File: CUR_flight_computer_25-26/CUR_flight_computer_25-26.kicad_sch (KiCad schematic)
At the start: 0 parts

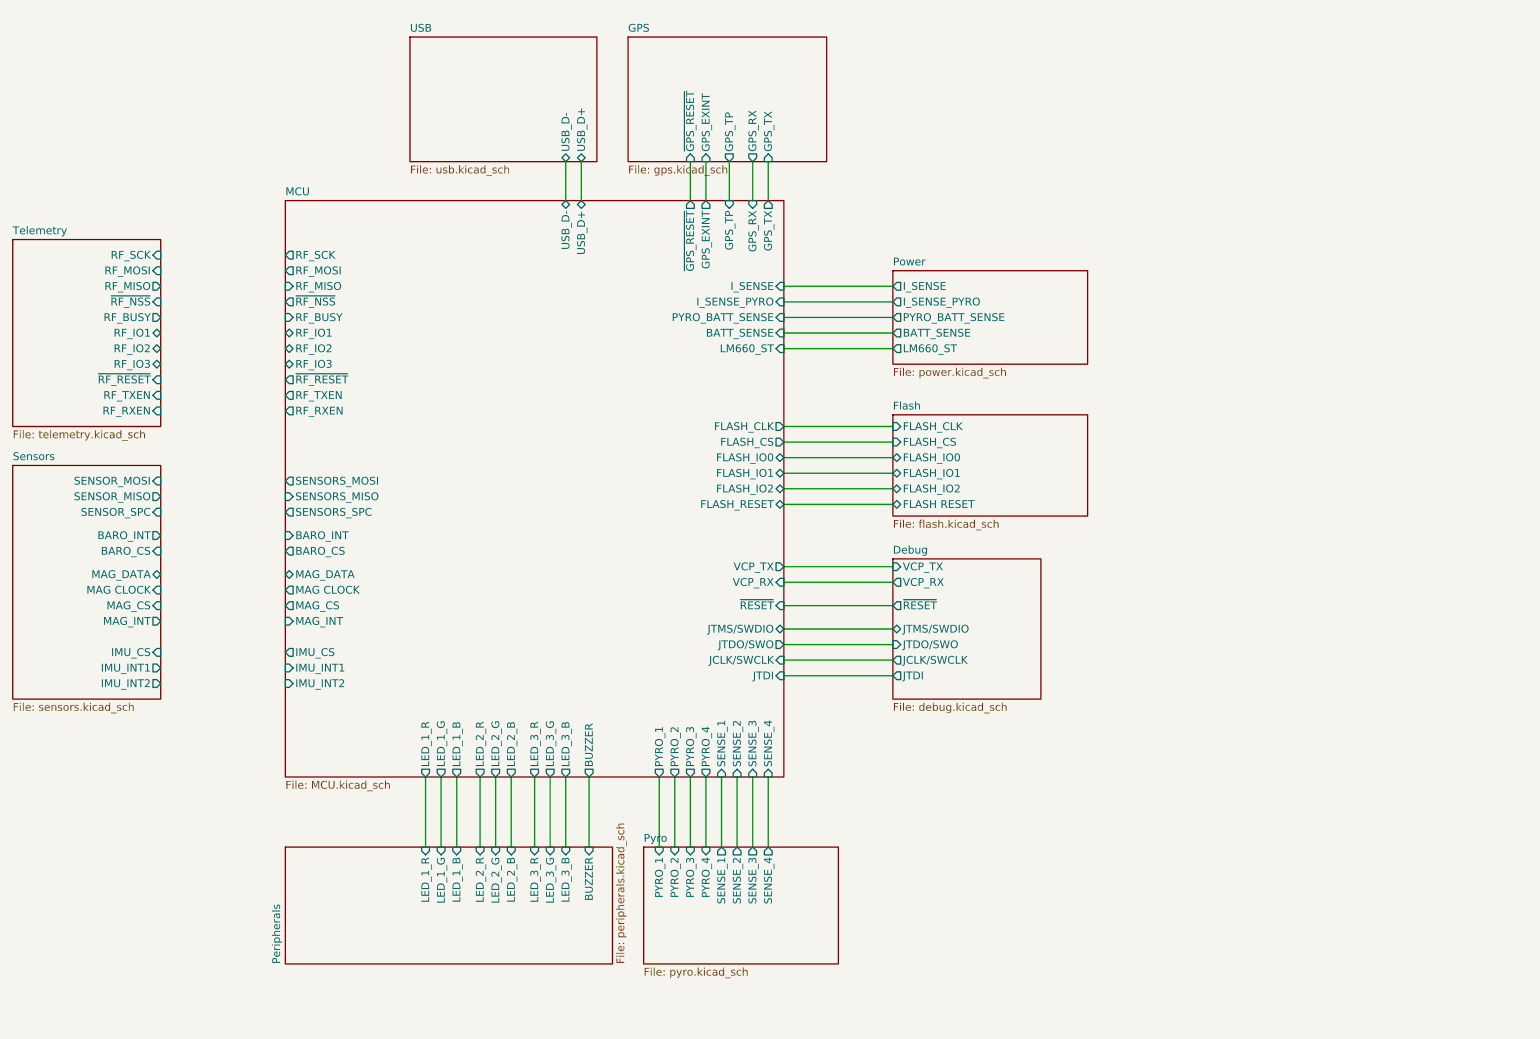
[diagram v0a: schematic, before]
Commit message: added SD_card holder
may need to confirm no pull up resistor required
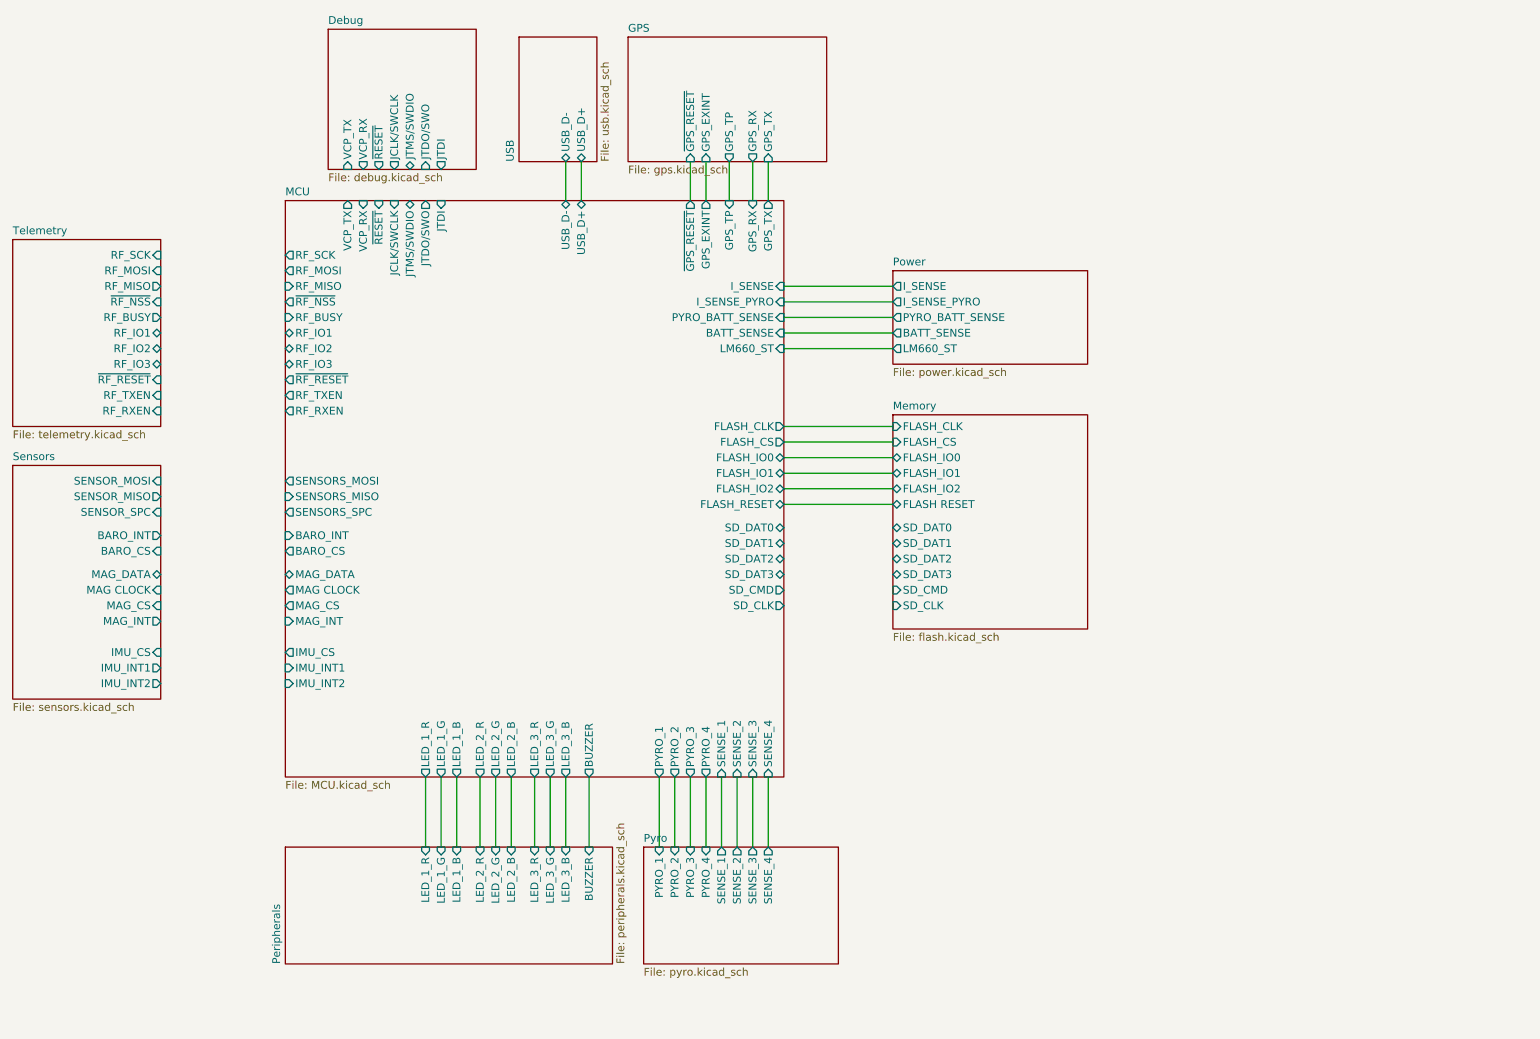
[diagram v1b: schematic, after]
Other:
- sheet Flash renamed Memory
- sheet MCU ports: added SD_CLK, SD_CMD, SD_DAT0, SD_DAT1, SD_DAT2, SD_DAT3; removed none
- sheet Memory ports: added SD_CLK, SD_CMD, SD_DAT0, SD_DAT1, SD_DAT2, SD_DAT3; removed none
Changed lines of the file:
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@@
-	(wire
-		(pts
-			(xy 162.56 105.41) (xy 180.34 105.41)
-		)
-		(stroke
-			(width 0)
-			(type default)
-		)
-	)
 	(wire
 		(pts
@@
 	(wire
 		(pts
-			(xy 162.56 111.76) (xy 180.34 111.76)
-		)
-		(stroke
-			(width 0)
-			(type default)
-		)
-	)
-	(wire
-		(pts
 			(xy 129.54 39.37) (xy 129.54 45.72)
 		)
@@
 	(wire
 		(pts
-			(xy 162.56 118.11) (xy 180.34 118.11)
-		)
-		(stroke
-			(width 0)
-			(type default)
-		)
-	)
-	(wire
-		(pts
 			(xy 124.46 139.7) (xy 124.46 151.13)
 		)
@@
 	(wire
 		(pts
-			(xy 162.56 123.19) (xy 180.34 123.19)
-		)
-		(stroke
-			(width 0)
-			(type default)
-		)
-	)
-	(wire
-		(pts
 			(xy 154.94 139.7) (xy 154.94 151.13)
 		)
@@
 	(wire
 		(pts
-			(xy 162.56 115.57) (xy 180.34 115.57)
-		)
-		(stroke
-			(width 0)
-			(type default)
-		)
-	)
-	(wire
-		(pts
 			(xy 180.34 59.69) (xy 162.56 59.69)
 		)
@@
 	(wire
 		(pts
-			(xy 162.56 120.65) (xy 180.34 120.65)
-		)
-		(stroke
-			(width 0)
-			(type default)
-		)
-	)
-	(wire
-		(pts
 			(xy 162.56 87.63) (xy 180.34 87.63)
 		)
@@
 	(wire
 		(pts
-			(xy 162.56 107.95) (xy 180.34 107.95)
-		)
-		(stroke
-			(width 0)
-			(type default)
-		)
-	)
-	(wire
-		(pts
 			(xy 127 139.7) (xy 127 151.13)
 		)
@@
 	)
 	(sheet
-		(at 180.34 104.14)
+		(at 88.265 17.78)
 		(size 24.13 22.86)
 		(exclude_from_sim no)
@@
 		)
 		(property "Sheetname" "Debug"
-			(at 180.34 103.4284 0)
+			(at 88.265 17.0684 0)
 			(effects
 				(font
@@
 		)
 		(property "Sheetfile" "debug.kicad_sch"
-			(at 180.34 127.5846 0)
+			(at 88.265 41.2246 0)
 			(effects
 				(font
@@
 		)
 		(pin "VCP_TX" input
-			(at 180.34 105.41 180)
+			(at 91.44 40.64 270)
 			(effects
 				(font
@@
 		)
 		(pin "JTDI" output
-			(at 180.34 123.19 180)
+			(at 106.68 40.64 270)
 			(effects
 				(font
@@
 		)
 		(pin "~{RESET}" output
-			(at 180.34 111.76 180)
+			(at 96.52 40.64 270)
 			(effects
 				(font
@@
 		)
 		(pin "JTMS/SWDIO" bidirectional
-			(at 180.34 115.57 180)
+			(at 101.6 40.64 270)
 			(effects
 				(font
@@
 		)
 		(pin "JTDO/SWO" input
-			(at 180.34 118.11 180)
+			(at 104.14 40.64 270)
 			(effects
 				(font
@@
 		)
 		(pin "JCLK/SWCLK" output
-			(at 180.34 120.65 180)
+			(at 99.06 40.64 270)
 			(effects
 				(font
@@
 		)
 		(pin "VCP_RX" output
-			(at 180.34 107.95 180)
+			(at 93.98 40.64 270)
 			(effects
 				(font
@@
 			)
 		)
-		(pin "VCP_TX" output
-			(at 162.56 105.41 0)
-			(effects
-				(font
-					(size 1.27 1.27)
-				)
-				(justify right)
-			)
-		)
-		(pin "JTDI" input
-			(at 162.56 123.19 0)
-			(effects
-				(font
-					(size 1.27 1.27)
-				)
-				(justify right)
-			)
-		)
-		(pin "~{RESET}" input
-			(at 162.56 111.76 0)
-			(effects
-				(font
-					(size 1.27 1.27)
-				)
-				(justify right)
-			)
-		)
-		(pin "JTMS/SWDIO" bidirectional
-			(at 162.56 115.57 0)
-			(effects
-				(font
-					(size 1.27 1.27)
-				)
-				(justify right)
-			)
-		)
-		(pin "JTDO{slash}SWO" output
-			(at 162.56 118.11 0)
-			(effects
-				(font
-					(size 1.27 1.27)
-				)
-				(justify right)
-			)
-		)
-		(pin "VCP_RX" input
-			(at 162.56 107.95 0)
-			(effects
-				(font
-					(size 1.27 1.27)
-				)
-				(justify right)
-			)
-		)
-		(pin "JCLK{slash}SWCLK" input
-			(at 162.56 120.65 0)
-			(effects
-				(font
-					(size 1.27 1.27)
-				)
-				(justify right)
-			)
-		)
 		(pin "LED_3_R" output
 			(at 121.92 139.7 270)
@@
 				)
 				(justify left)
+			)
+		)
+		(pin "JCLK{slash}SWCLK" input
+			(at 99.06 45.72 90)
+			(effects
+				(font
+					(size 1.27 1.27)
+				)
+				(justify right)
+			)
+		)
+		(pin "JTDI" input
+			(at 106.68 45.72 90)
+			(effects
+				(font
+					(size 1.27 1.27)
+				)
+				(justify right)
+			)
+		)
+		(pin "VCP_TX" output
+			(at 91.44 45.72 90)
+			(effects
+				(font
+					(size 1.27 1.27)
+				)
+				(justify right)
+			)
+		)
+		(pin "JTDO{slash}SWO" output
+			(at 104.14 45.72 90)
+			(effects
+				(font
+					(size 1.27 1.27)
+				)
+				(justify right)
+			)
+		)
+		(pin "JTMS/SWDIO" bidirectional
+			(at 101.6 45.72 90)
+			(effects
+				(font
+					(size 1.27 1.27)
+				)
+				(justify right)
+			)
+		)
+		(pin "~{RESET}" input
+			(at 96.52 45.72 90)
+			(effects
+				(font
+					(size 1.27 1.27)
+				)
+				(justify right)
+			)
+		)
+		(pin "VCP_RX" input
+			(at 93.98 45.72 90)
+			(effects
+				(font
+					(size 1.27 1.27)
+				)
+				(justify right)
+			)
+		)
+		(pin "SD_DAT3" bidirectional
+			(at 162.56 106.68 0)
+			(effects
+				(font
+					(size 1.27 1.27)
+				)
+				(justify right)
+			)
+		)
+		(pin "SD_DAT2" bidirectional
+			(at 162.56 104.14 0)
+			(effects
+				(font
+					(size 1.27 1.27)
+				)
+				(justify right)
+			)
+		)
+		(pin "SD_DAT1" bidirectional
+			(at 162.56 101.6 0)
+			(effects
+				(font
+					(size 1.27 1.27)
+				)
+				(justify right)
+			)
+		)
+		(pin "SD_CMD" output
+			(at 162.56 109.22 0)
+			(effects
+				(font
+					(size 1.27 1.27)
+				)
+				(justify right)
+			)
+		)
+		(pin "SD_DAT0" bidirectional
+			(at 162.56 99.06 0)
+			(effects
+				(font
+					(size 1.27 1.27)
+				)
+				(justify right)
+			)
+		)
+		(pin "SD_CLK" output
+			(at 162.56 111.76 0)
+			(effects
+				(font
+					(size 1.27 1.27)
+				)
+				(justify right)
 			)
 		)
@@
 	(sheet
 		(at 180.34 80.645)
-		(size 31.75 16.51)
+		(size 31.75 34.925)
 		(exclude_from_sim no)
 		(in_bom yes)
@@
 			(color 0 0 0 0.0000)
 		)
-		(property "Sheetname" "Flash"
+		(property "Sheetname" "Memory"
 			(at 180.34 79.9334 0)
 			(effects
@@
 		)
 		(property "Sheetfile" "flash.kicad_sch"
-			(at 180.34 97.7396 0)
+			(at 180.34 116.1546 0)
 			(effects
 				(font
@@
 		(pin "FLASH_IO1" bidirectional
 			(at 180.34 90.17 180)
+			(effects
+				(font
+					(size 1.27 1.27)
+				)
+				(justify left)
+			)
+		)
+		(pin "SD_DAT2" bidirectional
+			(at 180.34 104.14 180)
+			(effects
+				(font
+					(size 1.27 1.27)
+				)
+				(justify left)
+			)
+		)
+		(pin "SD_DAT3" bidirectional
+			(at 180.34 106.68 180)
+			(effects
+				(font
+					(size 1.27 1.27)
+				)
+				(justify left)
+			)
+		)
+		(pin "SD_DAT0" bidirectional
+			(at 180.34 99.06 180)
+			(effects
+				(font
+					(size 1.27 1.27)
+				)
+				(justify left)
+			)
+		)
+		(pin "SD_DAT1" bidirectional
+			(at 180.34 101.6 180)
+			(effects
+				(font
+					(size 1.27 1.27)
+				)
+				(justify left)
+			)
+		)
+		(pin "SD_CMD" input
+			(at 180.34 109.22 180)
+			(effects
+				(font
+					(size 1.27 1.27)
+				)
+				(justify left)
+			)
+		)
+		(pin "SD_CLK" input
+			(at 180.34 111.76 180)
 			(effects
 				(font
@@
 	)
 	(sheet
-		(at 101.6 19.05)
-		(size 30.48 20.32)
+		(at 119.38 19.05)
+		(size 12.7 20.32)
 		(exclude_from_sim no)
 		(in_bom yes)
@@
 		)
 		(property "Sheetname" "USB"
-			(at 101.6 18.3384 0)
+			(at 118.6684 39.37 90)
 			(effects
 				(font
@@
 		)
 		(property "Sheetfile" "usb.kicad_sch"
-			(at 101.6 39.9546 0)
-			(effects
-				(font
+			(at 132.6646 39.37 90)
+			(effects
+				(font

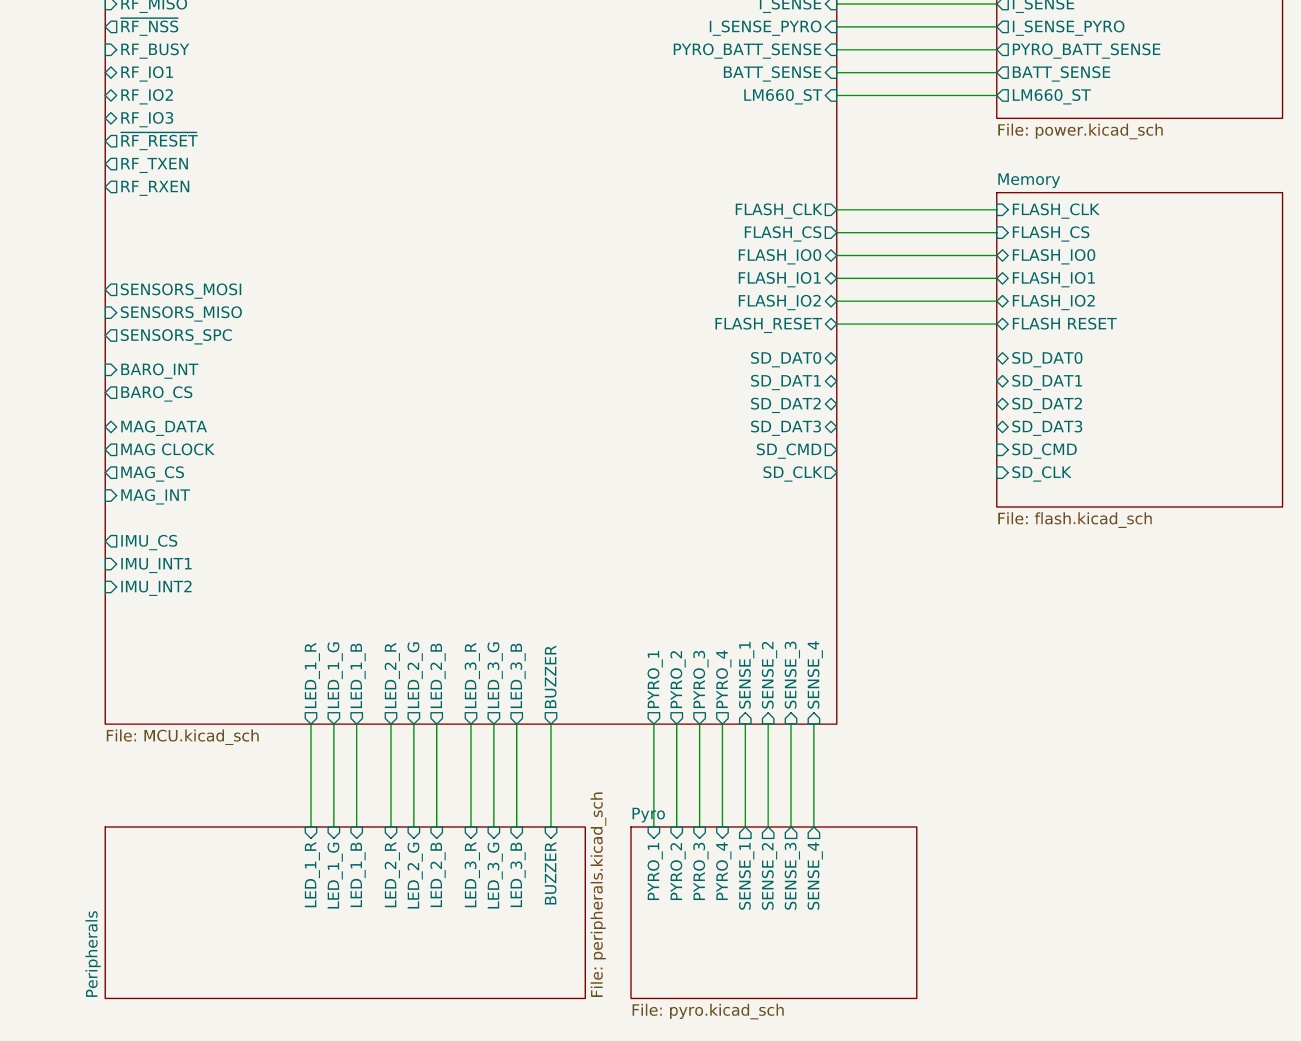
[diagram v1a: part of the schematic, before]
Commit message: hooked up more pins
added lcd header as well
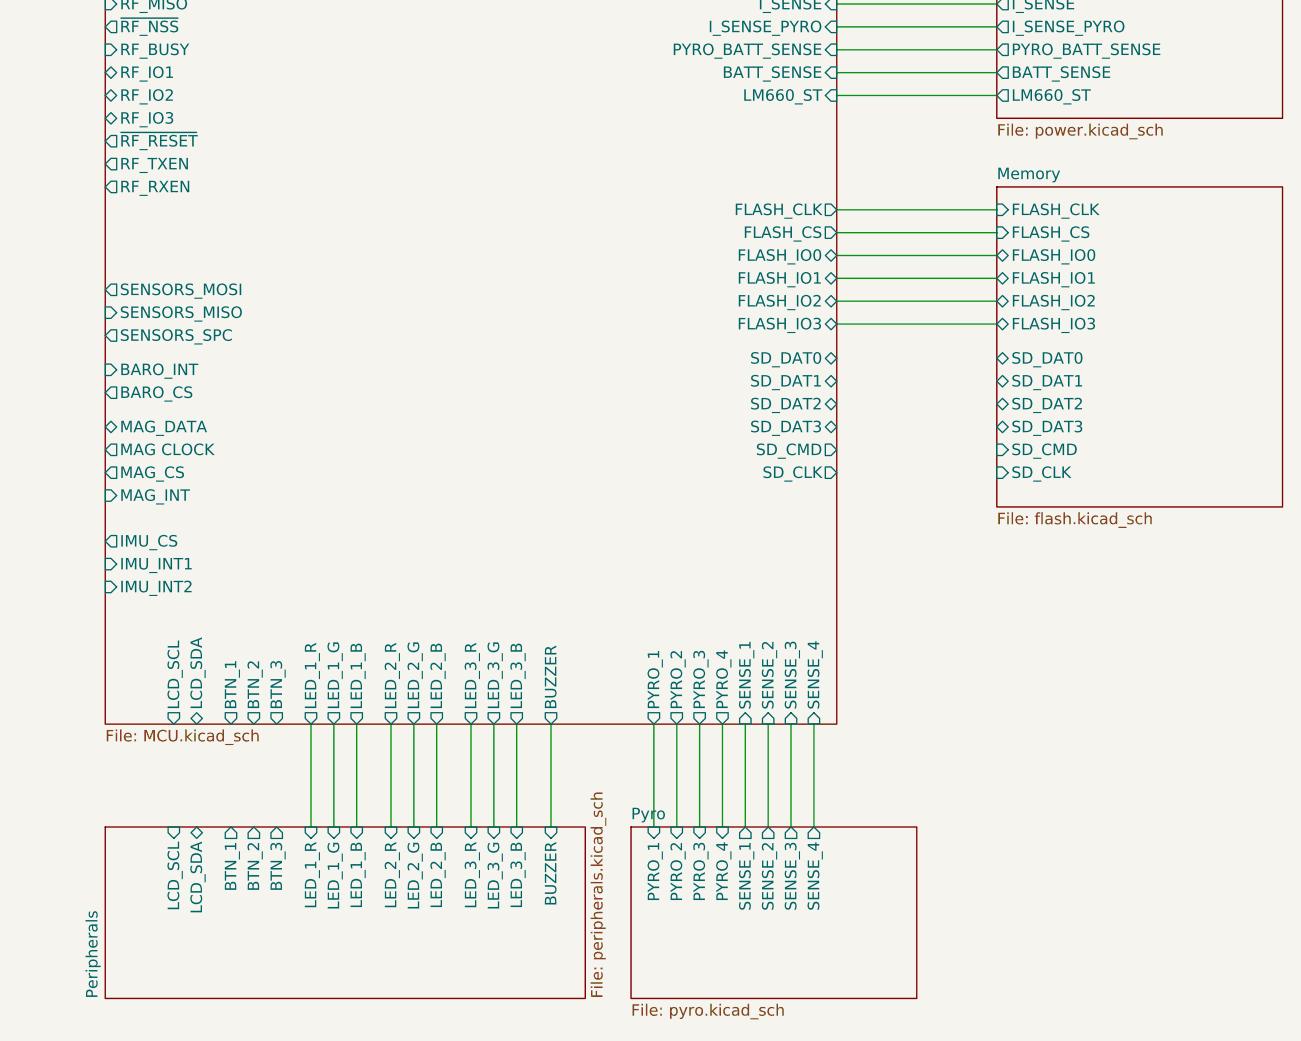
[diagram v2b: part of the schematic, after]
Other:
- sheet MCU ports: added BTN_1, BTN_2, BTN_3, FLASH_IO3, LCD_SCL, LCD_SDA; removed FLASH_RESET
- sheet Memory ports: added FLASH_IO3; removed FLASH RESET
- sheet Peripherals ports: added BTN_1, BTN_2, BTN_3, LCD_SCL, LCD_SDA; removed none
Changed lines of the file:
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@@
-			)
-		)
-		(pin "FLASH_RESET" bidirectional
-			(at 162.56 95.25 0)
-			(effects
-				(font
-					(size 1.27 1.27)
-				)
-				(justify right)
 			)
 		)
@@
 				)
 				(justify right)
+			)
+		)
+		(pin "LCD_SCL" output
+			(at 88.9 139.7 270)
+			(effects
+				(font
+					(size 1.27 1.27)
+				)
+				(justify left)
+			)
+		)
+		(pin "LCD_SDA" bidirectional
+			(at 91.44 139.7 270)
+			(effects
+				(font
+					(size 1.27 1.27)
+				)
+				(justify left)
+			)
+		)
+		(pin "BTN_1" output
+			(at 95.25 139.7 270)
+			(effects
+				(font
+					(size 1.27 1.27)
+				)
+				(justify left)
+			)
+		)
+		(pin "BTN_2" output
+			(at 97.79 139.7 270)
+			(effects
+				(font
+					(size 1.27 1.27)
+				)
+				(justify left)
+			)
+		)
+		(pin "FLASH_IO3" bidirectional
+			(at 162.56 95.25 0)
+			(effects
+				(font
+					(size 1.27 1.27)
+				)
+				(justify right)
+			)
+		)
+		(pin "BTN_3" output
+			(at 100.33 139.7 270)
+			(effects
+				(font
+					(size 1.27 1.27)
+				)
+				(justify left)
 			)
 		)
@@
 			)
 		)
+		(pin "BTN_2" output
+			(at 97.79 151.13 90)
+			(effects
+				(font
+					(size 1.27 1.27)
+				)
+				(justify right)
+			)
+		)
+		(pin "BTN_3" output
+			(at 100.33 151.13 90)
+			(effects
+				(font
+					(size 1.27 1.27)
+				)
+				(justify right)
+			)
+		)
+		(pin "BTN_1" output
+			(at 95.25 151.13 90)
+			(effects
+				(font
+					(size 1.27 1.27)
+				)
+				(justify right)
+			)
+		)
+		(pin "LCD_SDA" bidirectional
+			(at 91.44 151.13 90)
+			(effects
+				(font
+					(size 1.27 1.27)
+				)
+				(justify right)
+			)
+		)
+		(pin "LCD_SCL" input
+			(at 88.9 151.13 90)
+			(effects
+				(font
+					(size 1.27 1.27)
+				)
+				(justify right)
+			)
+		)
 		(instances
 			(project "CUR_flight_computer_25-26"
@@
 	)
 	(sheet
-		(at 180.34 80.645)
-		(size 31.75 34.925)
+		(at 180.34 80.01)
+		(size 31.75 35.56)
 		(exclude_from_sim no)
 		(in_bom yes)
@@
 		)
 		(property "Sheetname" "Memory"
-			(at 180.34 79.9334 0)
+			(at 180.34 79.2984 0)
 			(effects
 				(font
@@
 			)
 		)
-		(pin "FLASH RESET" bidirectional
-			(at 180.34 95.25 180)
-			(effects
-				(font
-					(size 1.27 1.27)
-				)
-				(justify left)
-			)
-		)
 		(pin "FLASH_CLK" input
 			(at 180.34 82.55 180)
@@
 			(effects
 				(font
+					(size 1.27 1.27)
+				)
+				(justify left)
+			)
+		)
+		(pin "FLASH_IO3" bidirectional
+			(at 180.34 95.25 180)
+			(effects
+				(font

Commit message: led fixes and such
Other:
- sheet MCU ports: added none; removed RF_IO3
- sheet Telemetry ports: added none; removed RF_IO3
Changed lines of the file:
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@@
-			)
-		)
-		(pin "RF_IO3" bidirectional
-			(at 60.96 72.39 0)
-			(effects
-				(font
-					(size 1.27 1.27)
-				)
-				(justify right)
 			)
 		)
@@
 			(effects
 				(font
-					(size 1.27 1.27)
-				)
-				(justify left)
-			)
-		)
-		(pin "RF_IO3" bidirectional
-			(at 81.28 72.39 180)
-			(effects
-				(font
